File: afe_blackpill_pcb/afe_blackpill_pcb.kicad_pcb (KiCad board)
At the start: 2 copper layers, 68.8 x 62.3 mm, 2 parts, among them J6 pinheader_2x6_socket, U10 BlackPill_F4_SWI

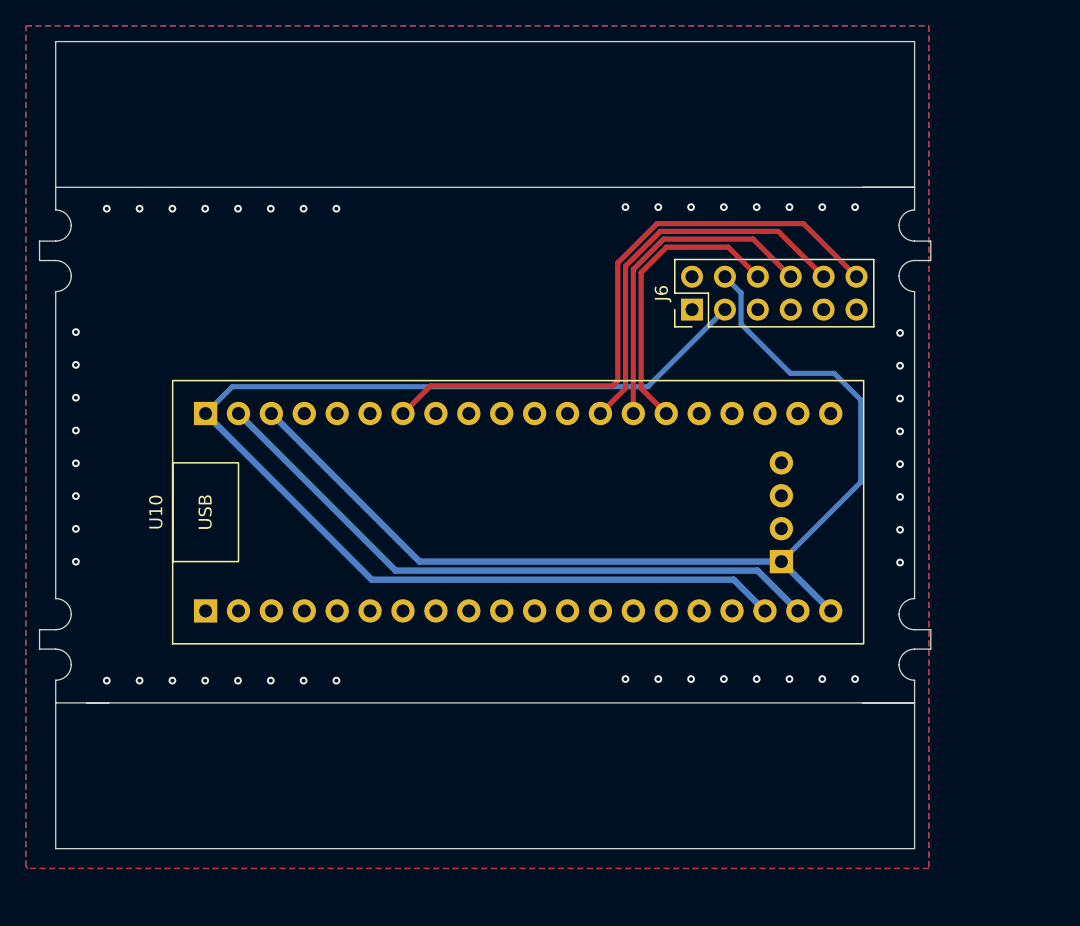
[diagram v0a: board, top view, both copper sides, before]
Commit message: fixed hbus location, added bc71,6 edgecuts'
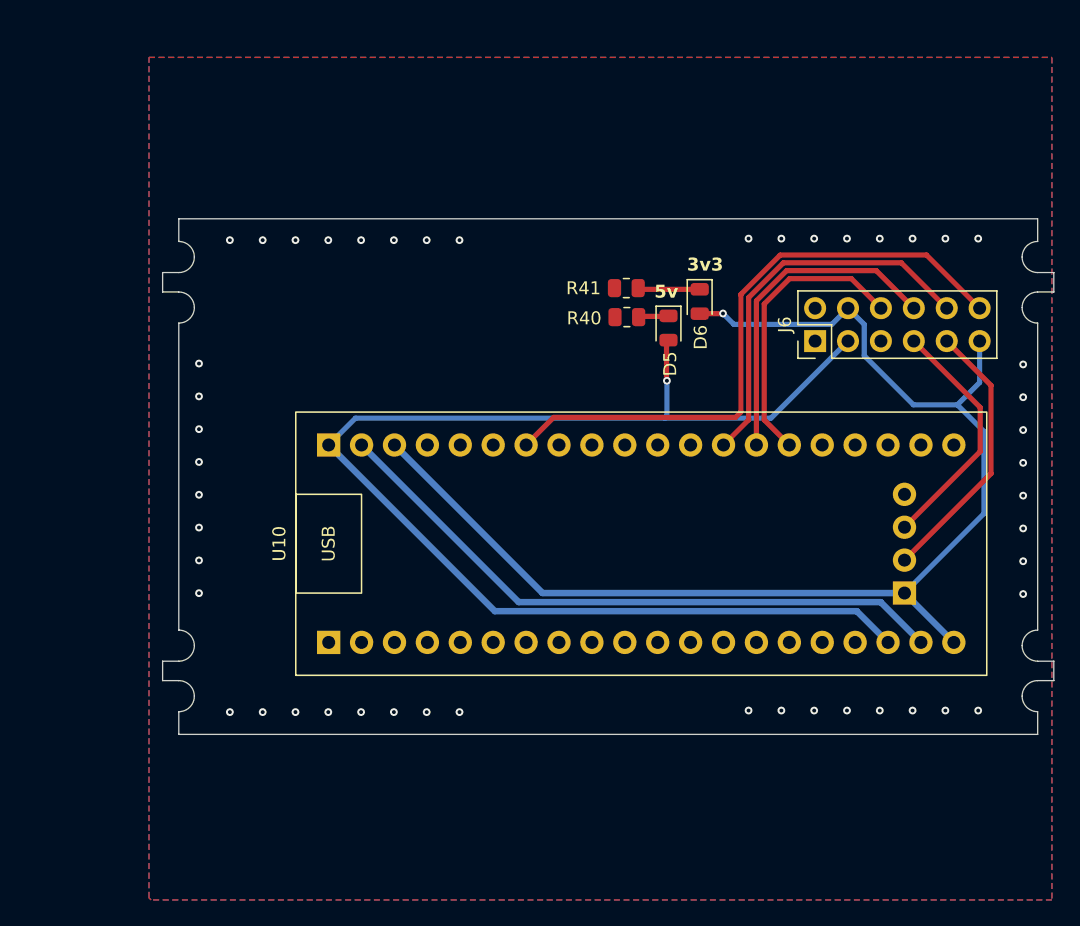
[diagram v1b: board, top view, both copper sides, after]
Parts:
- added D5: LED, LED_SMD:LED_0805_2012Metric, F.Cu at (155.0, 84.4)
- added D6: LED, LED_SMD:LED_0805_2012Metric, F.Cu at (157.4, 82.4)
- added R40: 2.2k, Resistor_SMD:R_0805_2012Metric, F.Cu at (151.8, 83.6)
- added R41: 2.2k, Resistor_SMD:R_0805_2012Metric, F.Cu at (151.7, 81.3)
- moved J6 9.81 mm to (166.3, 85.4)
- moved U10 9.81 mm to (128.8, 108.7)
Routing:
- net (no net): track 348.8 -> 419.8 mm, vias 48 -> 50
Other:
- board size 68.8 x 62.3 mm -> 68.8 x 39.8 mm
- board text added: "3v3"
- board text added: "5v"
